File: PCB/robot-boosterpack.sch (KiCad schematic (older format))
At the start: 2 parts

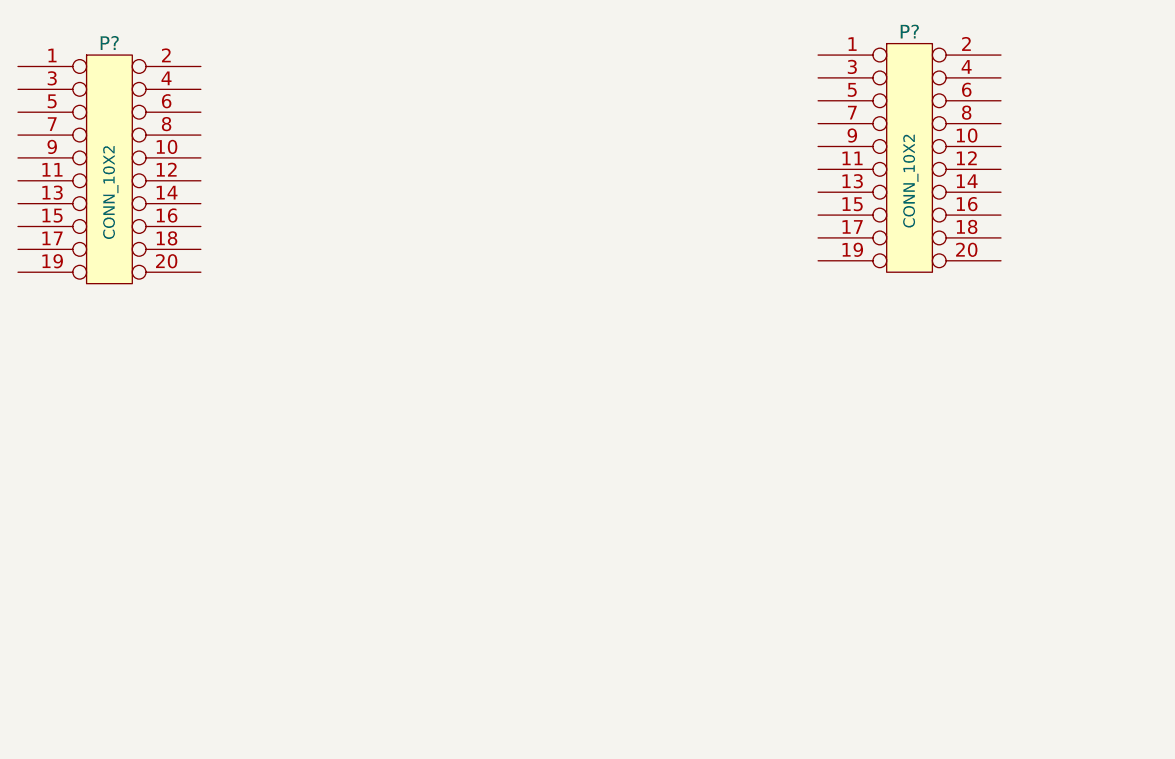
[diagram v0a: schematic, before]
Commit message: added libraries for motor driver, motor, and IR
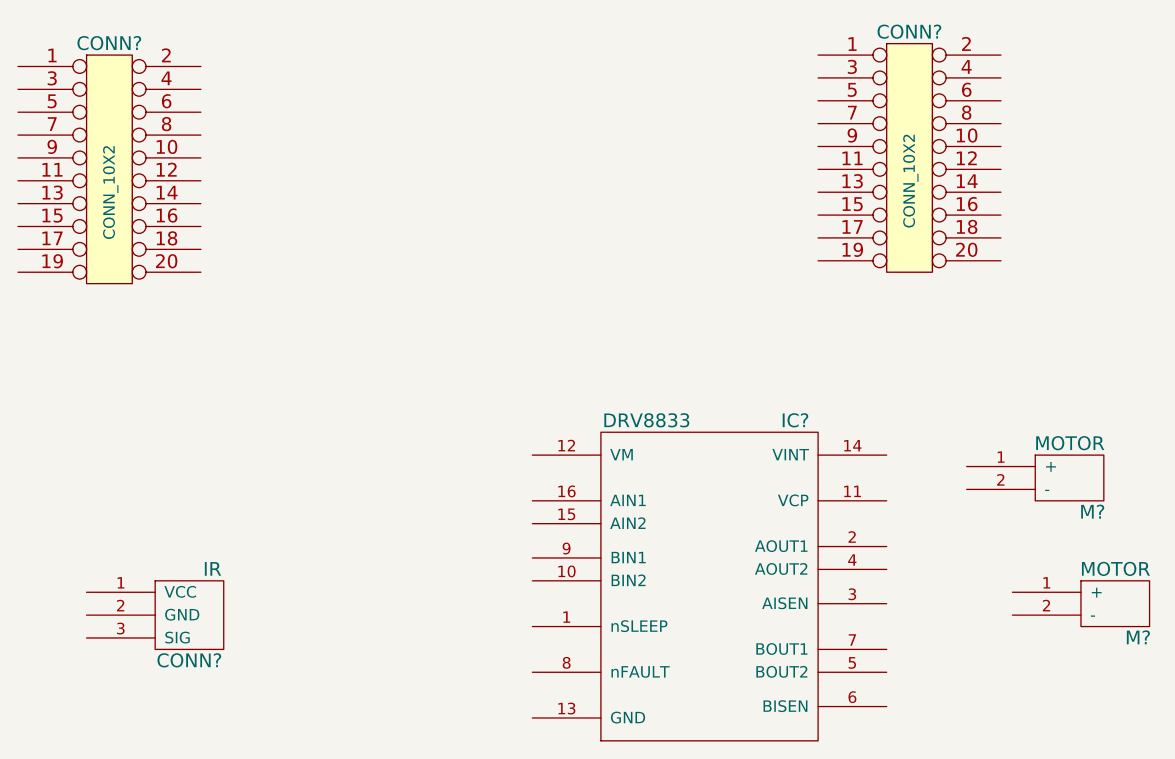
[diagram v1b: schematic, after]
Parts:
- added CONN?: IR, symbol IR
- added IC?: DRV8833, ~, symbol DRV8833
- added M? (x2): MOTOR, symbol MOTOR
- gave numbers to parts that had none: 1
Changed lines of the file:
@@
 LIBS:contrib
 LIBS:valves
-EELAYER 24 0
+LIBS:robot-boosterpack
+LIBS:robot-boosterpack-cache
+EELAYER 27 0
 EELAYER END
 $Descr A4 11693 8268
@@
 Sheet 1 1
 Title ""
-Date ""
+Date "22 jun 2014"
 Rev ""
 Comp ""
@@
 $EndDescr
 $Comp
-L CONN_10X2 P?
+L CONN_10X2 CONN?
 U 1 1 53A20530
 P 4000 3600
-F 0 "P?" H 4000 4150 60  0000 C CNN
+F 0 "CONN?" H 4000 4150 60  0000 C CNN
 F 1 "CONN_10X2" V 4000 3500 50  0000 C CNN
 F 2 "" H 4000 3600 60  0000 C CNN
@@
 $EndComp
 $Comp
-L CONN_10X2 P?
+L CONN_10X2 CONN?
 U 1 1 53A205F9
 P 7500 3550
-F 0 "P?" H 7500 4100 60  0000 C CNN
+F 0 "CONN?" H 7500 4100 60  0000 C CNN
 F 1 "CONN_10X2" V 7500 3450 50  0000 C CNN
 F 2 "" H 7500 3550 60  0000 C CNN
@@
 	1    0    0    -1
 $EndComp
+$Comp
+L DRV8833 IC?
+U 1 1 53A71BC8
+P 6600 5350
+F 0 "IC?" H 7000 6000 60  0000 C CNN
+F 1 "DRV8833" H 6350 6000 60  0000 C CNN
+F 2 "~" H 6350 6000 60  0000 C CNN
+F 3 "~" H 6350 6000 60  0000 C CNN
+	1    6600 5350
+	1    0    0    -1
+$EndComp
+$Comp
+L MOTOR M?
+U 1 1 53A71E5E
+P 8200 4950
+F 0 "M?" H 8300 4800 60  0000 C CNN
+F 1 "MOTOR" H 8200 5100 60  0000 C CNN
+F 2 "" H 8000 5150 60  0000 C CNN
+F 3 "" H 8000 5150 60  0000 C CNN
+	1    8200 4950
+	1    0    0    -1
+$EndComp
+$Comp
+L MOTOR M?
+U 1 1 53A71E6D
+P 8400 5500
+F 0 "M?" H 8500 5350 60  0000 C CNN
+F 1 "MOTOR" H 8400 5650 60  0000 C CNN
+F 2 "" H 8200 5700 60  0000 C CNN
+F 3 "" H 8200 5700 60  0000 C CNN
+	1    8400 5500
+	1    0    0    -1
+$EndComp
+$Comp
+L IR CONN?
+U 1 1 53A7290D
+P 4400 5550
+F 0 "CONN?" H 4350 5350 60  0000 C CNN
+F 1 "IR" H 4450 5750 60  0000 C CNN
+F 2 "" H 4450 5750 60  0000 C CNN
+F 3 "" H 4450 5750 60  0000 C CNN
+	1    4400 5550
+	1    0    0    -1
+$EndComp

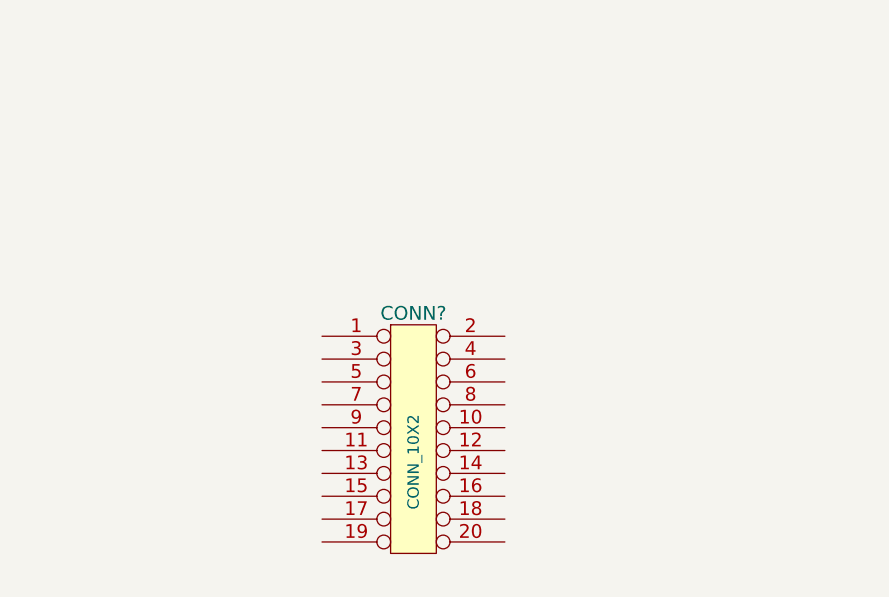
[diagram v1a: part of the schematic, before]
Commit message: added reflectance sensor
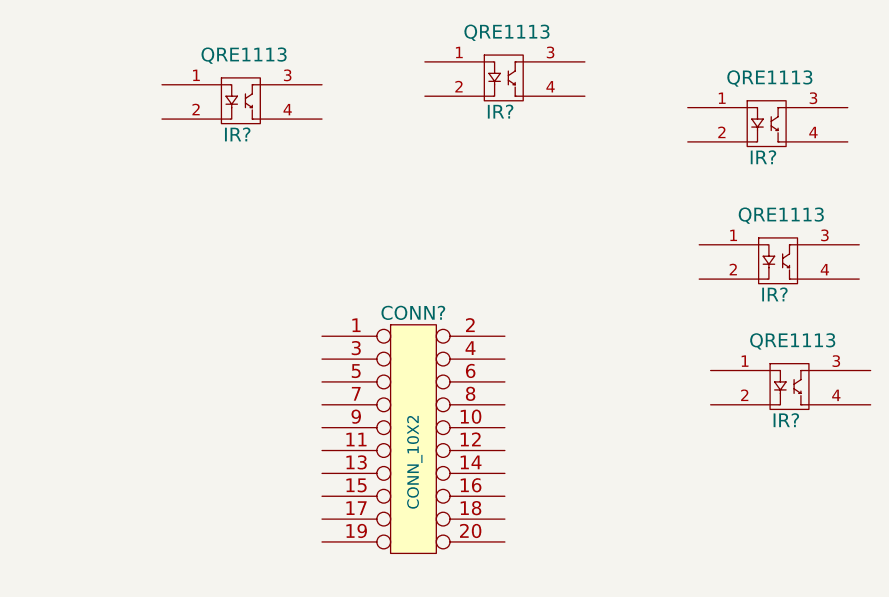
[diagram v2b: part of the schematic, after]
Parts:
- added IR? (x5): QRE1113, symbol QRE1113
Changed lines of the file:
@@
+	1    0    0    -1
+$EndComp
+$Comp
+L QRE1113 IR?
+U 1 1 53A7351D
+P 6750 2050
+F 0 "IR?" H 6730 1880 60  0000 C CNN
+F 1 "QRE1113" H 6760 2230 60  0000 C CNN
+F 2 "" H 6760 2230 60  0000 C CNN
+F 3 "" H 6760 2230 60  0000 C CNN
+	1    6750 2050
+	1    0    0    -1
+$EndComp
+$Comp
+L QRE1113 IR?
+U 1 1 53A7352C
+P 7900 1950
+F 0 "IR?" H 7880 1780 60  0000 C CNN
+F 1 "QRE1113" H 7910 2130 60  0000 C CNN
+F 2 "" H 7910 2130 60  0000 C CNN
+F 3 "" H 7910 2130 60  0000 C CNN
+	1    7900 1950
+	1    0    0    -1
+$EndComp
+$Comp
+L QRE1113 IR?
+U 1 1 53A7353B
+P 9050 2150
+F 0 "IR?" H 9030 1980 60  0000 C CNN
+F 1 "QRE1113" H 9060 2330 60  0000 C CNN
+F 2 "" H 9060 2330 60  0000 C CNN
+F 3 "" H 9060 2330 60  0000 C CNN
+	1    9050 2150
+	1    0    0    -1
+$EndComp
+$Comp
+L QRE1113 IR?
+U 1 1 53A7354A
+P 9100 2750
+F 0 "IR?" H 9080 2580 60  0000 C CNN
+F 1 "QRE1113" H 9110 2930 60  0000 C CNN
+F 2 "" H 9110 2930 60  0000 C CNN
+F 3 "" H 9110 2930 60  0000 C CNN
+	1    9100 2750
+	1    0    0    -1
+$EndComp
+$Comp
+L QRE1113 IR?
+U 1 1 53A73559
+P 9150 3300
+F 0 "IR?" H 9130 3130 60  0000 C CNN
+F 1 "QRE1113" H 9160 3480 60  0000 C CNN
+F 2 "" H 9160 3480 60  0000 C CNN
+F 3 "" H 9160 3480 60  0000 C CNN
+	1    9150 3300
 	1    0    0    -1
 $EndComp

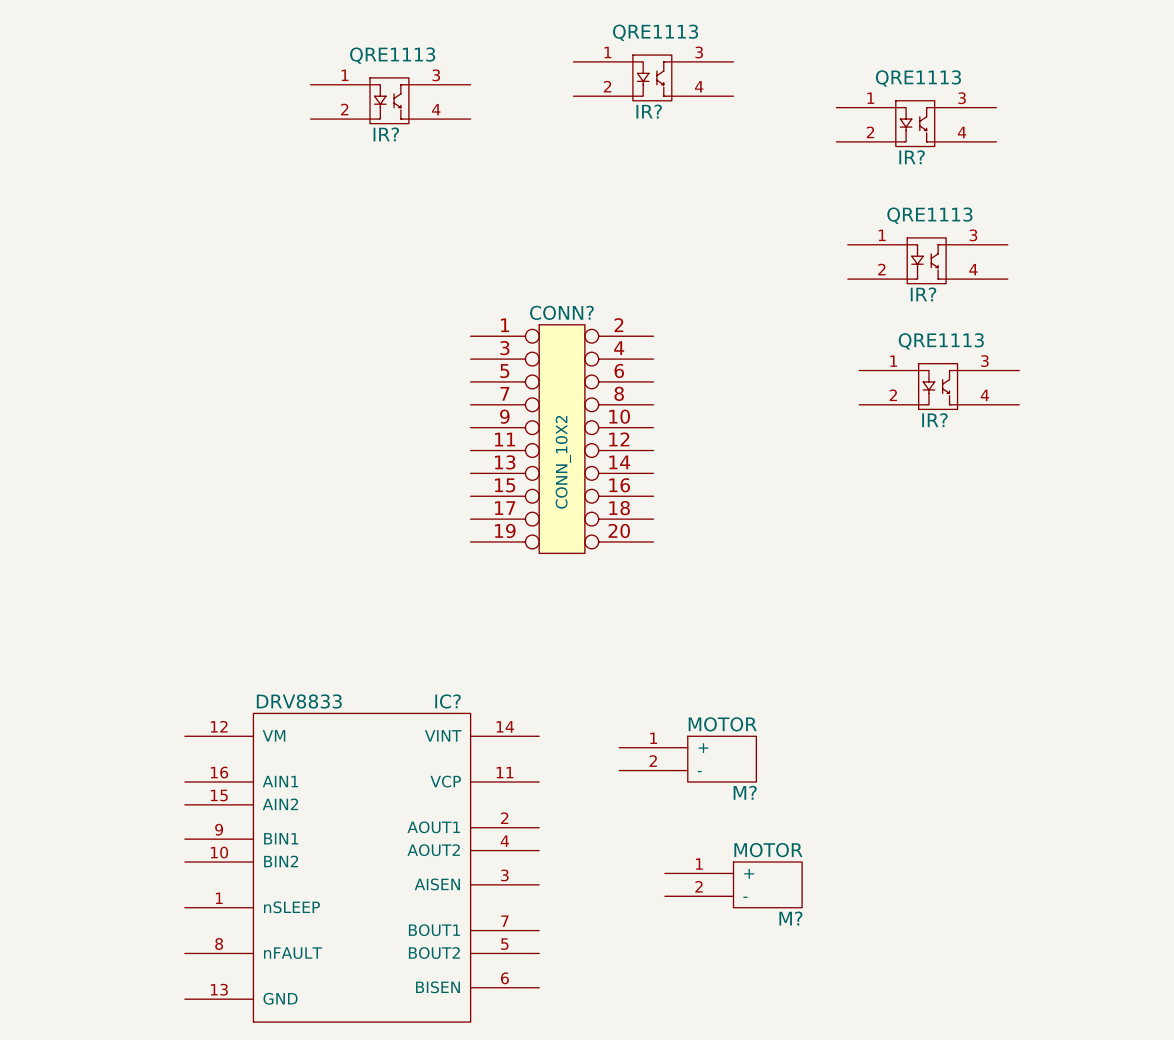
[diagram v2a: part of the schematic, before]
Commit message: added battery holder
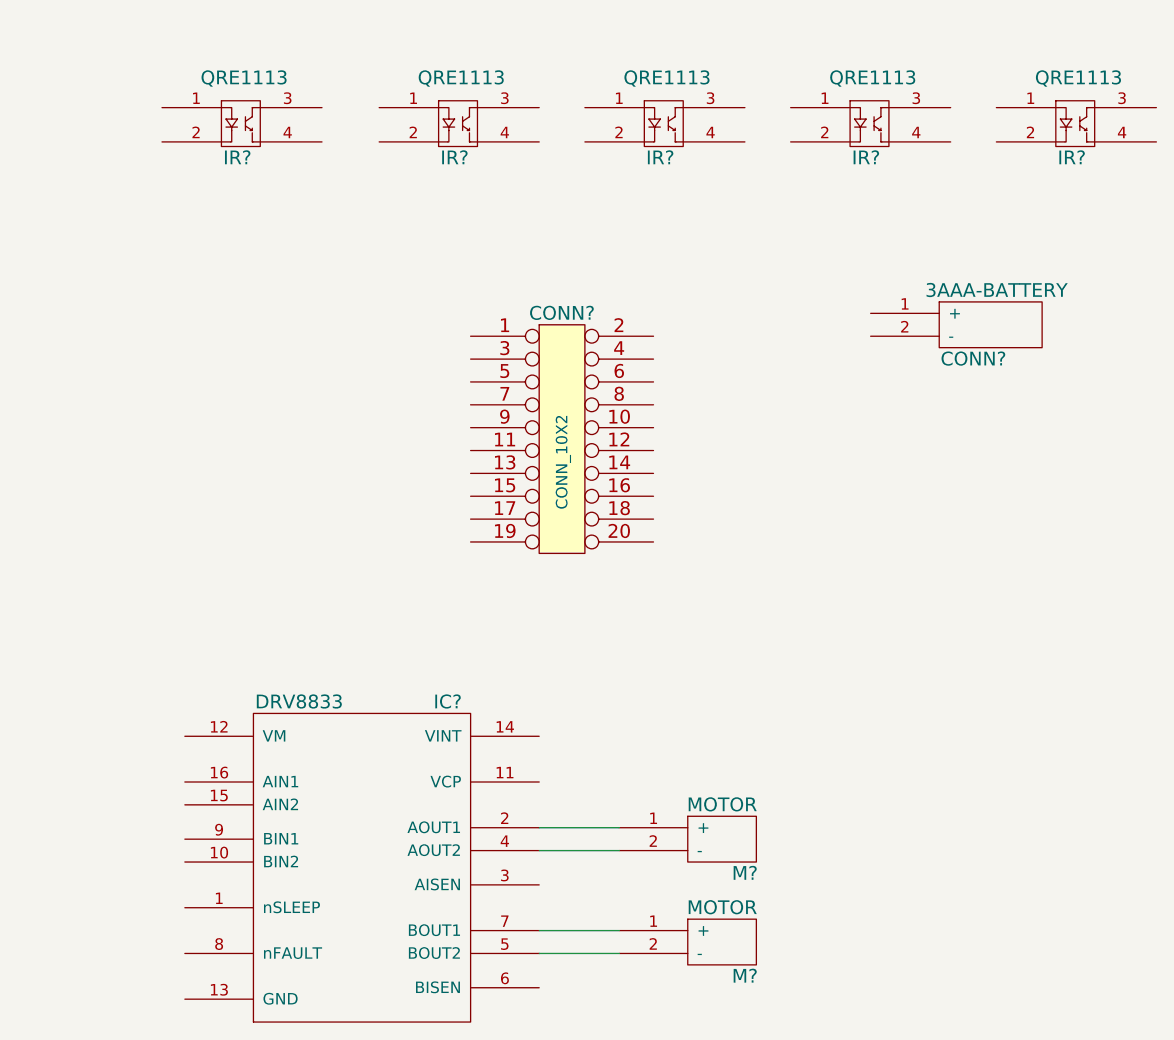
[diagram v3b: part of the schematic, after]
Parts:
- added CONN?: 3AAA-BATTERY, symbol 3AAA-BATTERY
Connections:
- net at IC?.2 (AOUT1): now also M?.1 (+)
- net at IC?.4 (AOUT2): now also M?.2 (-)
- net at IC?.5 (BOUT2): now also M?.2 (-)
- net at IC?.7 (BOUT1): now also M?.1 (+)
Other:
- moved on the sheet: IR?, M?
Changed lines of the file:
@@
 L MOTOR M?
 U 1 1 53A71E5E
-P 8200 4950
-F 0 "M?" H 8300 4800 60  0000 C CNN
-F 1 "MOTOR" H 8200 5100 60  0000 C CNN
-F 2 "" H 8000 5150 60  0000 C CNN
-F 3 "" H 8000 5150 60  0000 C CNN
-	1    8200 4950
+P 8200 5300
+F 0 "M?" H 8300 5150 60  0000 C CNN
+F 1 "MOTOR" H 8200 5450 60  0000 C CNN
+F 2 "" H 8000 5500 60  0000 C CNN
+F 3 "" H 8000 5500 60  0000 C CNN
+	1    8200 5300
 	1    0    0    -1
 $EndComp
@@
 L MOTOR M?
 U 1 1 53A71E6D
-P 8400 5500
-F 0 "M?" H 8500 5350 60  0000 C CNN
-F 1 "MOTOR" H 8400 5650 60  0000 C CNN
-F 2 "" H 8200 5700 60  0000 C CNN
-F 3 "" H 8200 5700 60  0000 C CNN
-	1    8400 5500
+P 8200 5750
+F 0 "M?" H 8300 5600 60  0000 C CNN
+F 1 "MOTOR" H 8200 5900 60  0000 C CNN
+F 2 "" H 8000 5950 60  0000 C CNN
+F 3 "" H 8000 5950 60  0000 C CNN
+	1    8200 5750
 	1    0    0    -1
 $EndComp
@@
 L QRE1113 IR?
 U 1 1 53A7351D
-P 6750 2050
-F 0 "IR?" H 6730 1880 60  0000 C CNN
-F 1 "QRE1113" H 6760 2230 60  0000 C CNN
-F 2 "" H 6760 2230 60  0000 C CNN
-F 3 "" H 6760 2230 60  0000 C CNN
-	1    6750 2050
+P 6100 2150
+F 0 "IR?" H 6080 1980 60  0000 C CNN
+F 1 "QRE1113" H 6110 2330 60  0000 C CNN
+F 2 "" H 6110 2330 60  0000 C CNN
+F 3 "" H 6110 2330 60  0000 C CNN
+	1    6100 2150
 	1    0    0    -1
 $EndComp
@@
 L QRE1113 IR?
 U 1 1 53A7352C
-P 7900 1950
-F 0 "IR?" H 7880 1780 60  0000 C CNN
-F 1 "QRE1113" H 7910 2130 60  0000 C CNN
-F 2 "" H 7910 2130 60  0000 C CNN
-F 3 "" H 7910 2130 60  0000 C CNN
-	1    7900 1950
+P 7050 2150
+F 0 "IR?" H 7030 1980 60  0000 C CNN
+F 1 "QRE1113" H 7060 2330 60  0000 C CNN
+F 2 "" H 7060 2330 60  0000 C CNN
+F 3 "" H 7060 2330 60  0000 C CNN
+	1    7050 2150
 	1    0    0    -1
 $EndComp
@@
 L QRE1113 IR?
 U 1 1 53A7353B
-P 9050 2150
-F 0 "IR?" H 9030 1980 60  0000 C CNN
-F 1 "QRE1113" H 9060 2330 60  0000 C CNN
-F 2 "" H 9060 2330 60  0000 C CNN
-F 3 "" H 9060 2330 60  0000 C CNN
-	1    9050 2150
+P 7950 2150
+F 0 "IR?" H 7930 1980 60  0000 C CNN
+F 1 "QRE1113" H 7960 2330 60  0000 C CNN
+F 2 "" H 7960 2330 60  0000 C CNN
+F 3 "" H 7960 2330 60  0000 C CNN
+	1    7950 2150
 	1    0    0    -1
 $EndComp
@@
 L QRE1113 IR?
 U 1 1 53A7354A
-P 9100 2750
-F 0 "IR?" H 9080 2580 60  0000 C CNN
-F 1 "QRE1113" H 9110 2930 60  0000 C CNN
-F 2 "" H 9110 2930 60  0000 C CNN
-F 3 "" H 9110 2930 60  0000 C CNN
-	1    9100 2750
+P 8850 2150
+F 0 "IR?" H 8830 1980 60  0000 C CNN
+F 1 "QRE1113" H 8860 2330 60  0000 C CNN
+F 2 "" H 8860 2330 60  0000 C CNN
+F 3 "" H 8860 2330 60  0000 C CNN
+	1    8850 2150
 	1    0    0    -1
 $EndComp
@@
 L QRE1113 IR?
 U 1 1 53A73559
-P 9150 3300
-F 0 "IR?" H 9130 3130 60  0000 C CNN
-F 1 "QRE1113" H 9160 3480 60  0000 C CNN
-F 2 "" H 9160 3480 60  0000 C CNN
-F 3 "" H 9160 3480 60  0000 C CNN
-	1    9150 3300
+P 9750 2150
+F 0 "IR?" H 9730 1980 60  0000 C CNN
+F 1 "QRE1113" H 9760 2330 60  0000 C CNN
+F 2 "" H 9760 2330 60  0000 C CNN
+F 3 "" H 9760 2330 60  0000 C CNN
+	1    9750 2150
 	1    0    0    -1
 $EndComp
+Wire Wire Line
+	7400 5250 7750 5250
+Wire Wire Line
+	7400 5350 7750 5350
+Wire Wire Line
+	7400 5700 7750 5700
+Wire Wire Line
+	7400 5800 7750 5800
+$Comp
+L 3AAA-BATTERY CONN?
+U 1 1 53A73812
+P 9350 3050
+F 0 "CONN?" H 9300 2900 60  0000 C CNN
+F 1 "3AAA-BATTERY" H 9400 3200 60  0000 C CNN
+F 2 "" H 8850 3200 60  0000 C CNN
+F 3 "" H 8850 3200 60  0000 C CNN
+	1    9350 3050
+	1    0    0    -1
+$EndComp
